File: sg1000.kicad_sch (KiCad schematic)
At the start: 65 parts, among them CN1 Conn_01x07_Female, J1 USB-B1HSB6, J2 RCJ-014, J3 RCJ-013, Q1 2n4401, Q1c1 2n3906, SW1 Pause Key, SW2 Power Toggle, U1 SG-1000-Cart, U10 PLCCZ80, U100 74HCT574, U101 74HCT574, U102 74HCT574, U103 AS6C62256-DIP, U11 AS6C62256-DIP, U12 TMS9918A, U13 74LS139, U16 74LS32, U18 74LS257, U2 SG-1000-Expansion, U21 74LS257, U3 SN76489AN, U99 74HCT04, X2 10.73863MHz

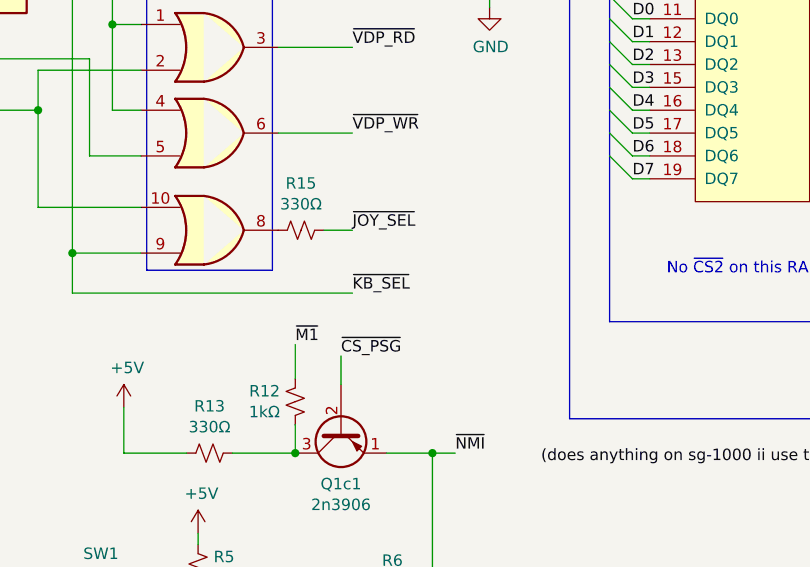
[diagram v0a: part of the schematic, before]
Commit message: Hook up KBSEL
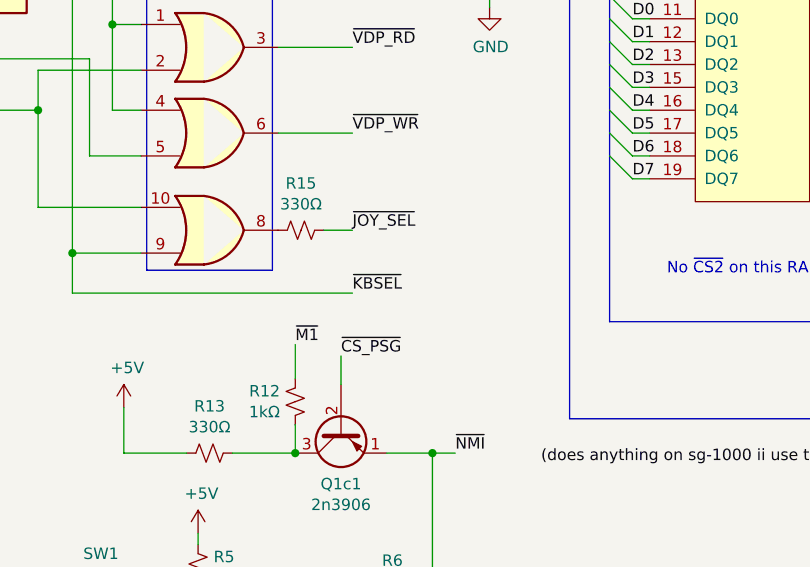
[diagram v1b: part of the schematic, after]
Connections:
- net ~{KB_SEL} is gone; now on net ~{KBSEL}: U13.9 (O3), U16.9
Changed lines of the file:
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@@
     (effects (font (size 1.27 1.27)) (justify right bottom))
   )
-  (label "~{KB_SEL}" (at 111.125 147.32 0)
+  (label "~{KBSEL}" (at 111.125 147.32 0)
     (effects (font (size 1.27 1.27)) (justify left bottom))
   )

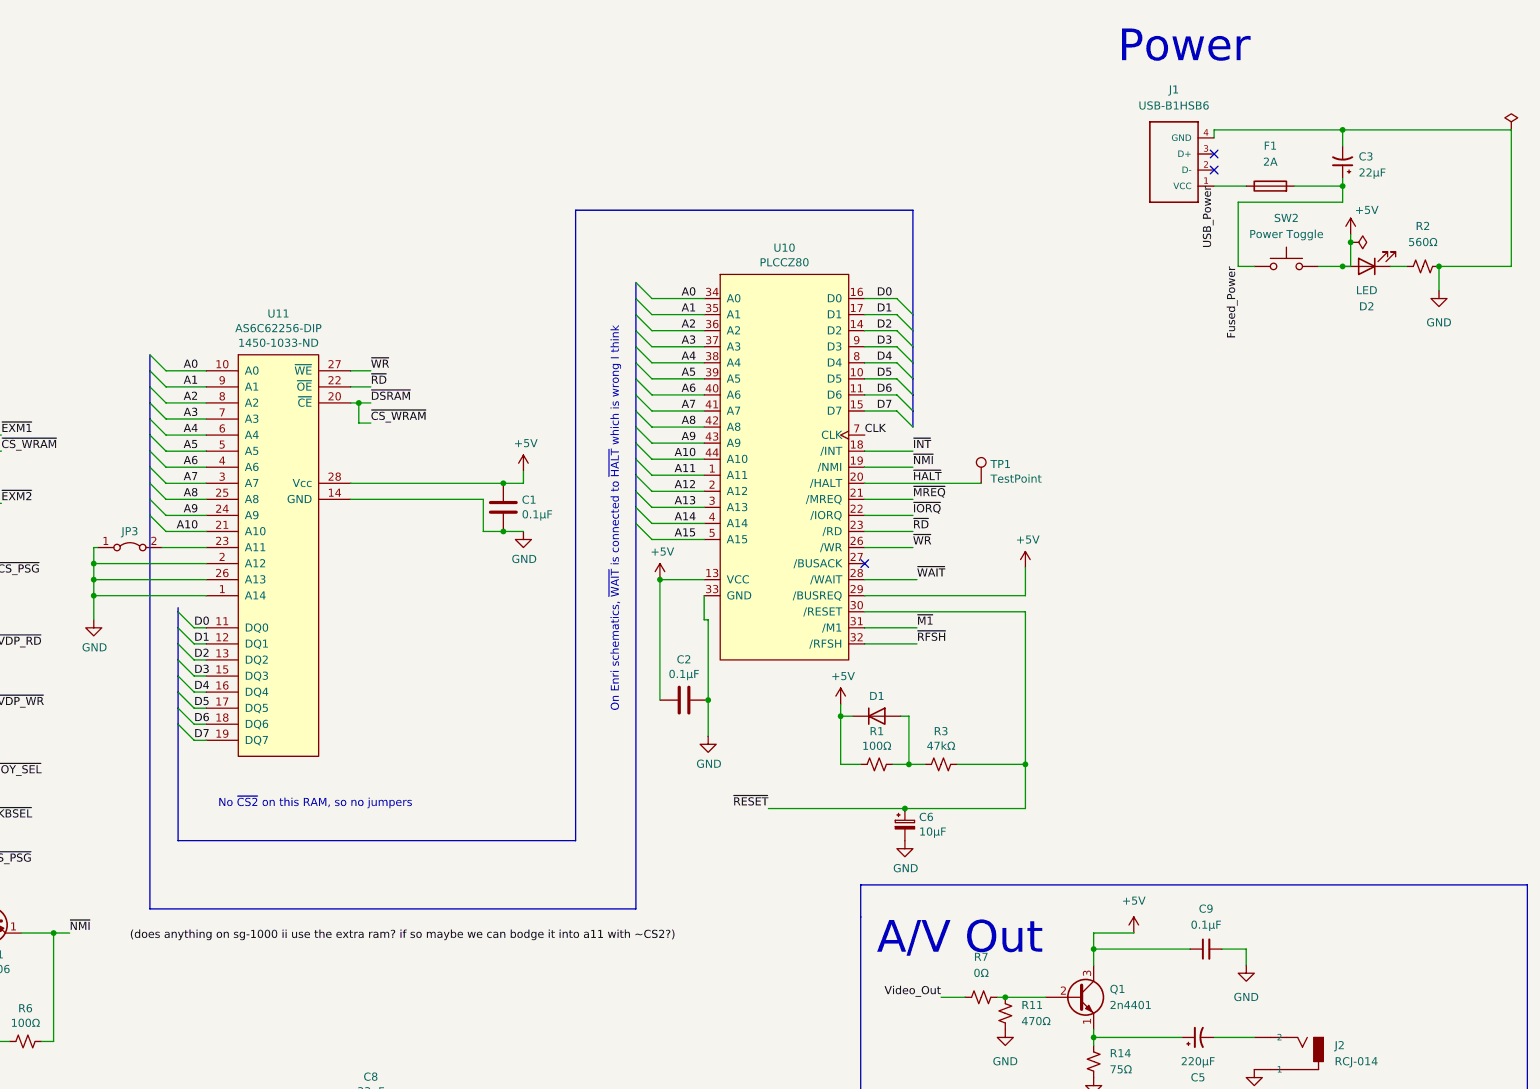
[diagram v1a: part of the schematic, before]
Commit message: Fix many pin warnings
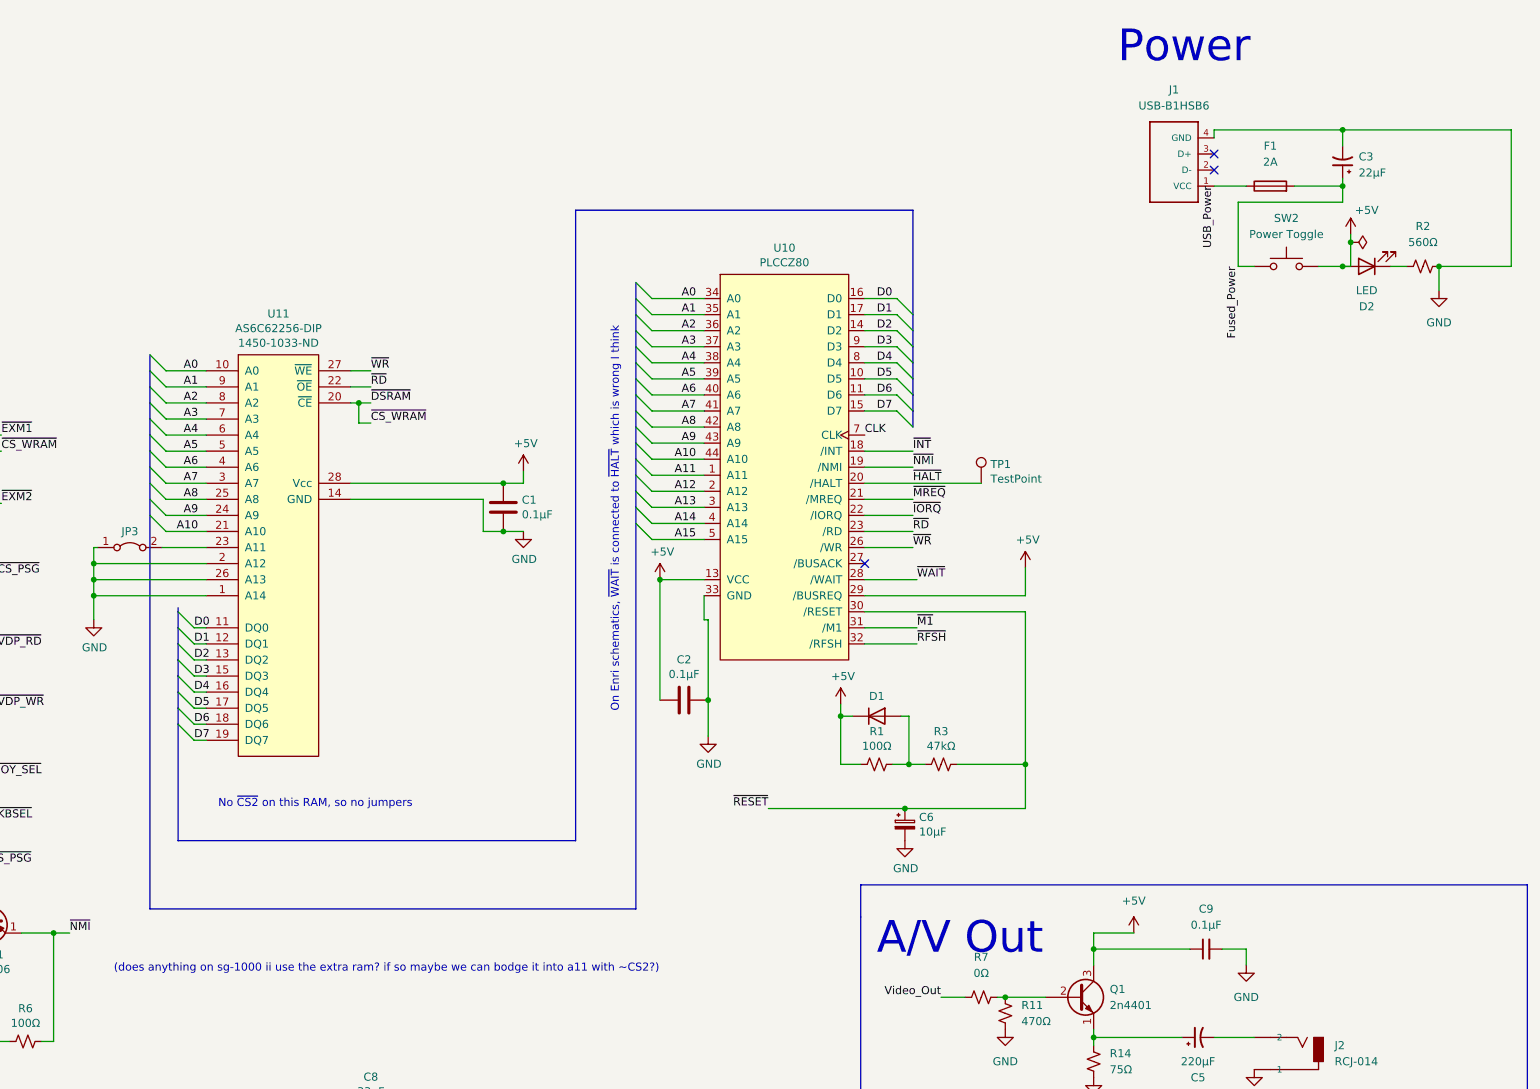
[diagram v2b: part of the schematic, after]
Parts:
- J1: footprint USB-B1HSB6:OST_USB-B1HSB6 -> OST_USB-B1HSB6
- U103, U11: footprint Package_DIP:DIP-28_W15.24mm_Socket_LongPads -> Housings_DIP:DIP-28_W15.24mm_Socket_LongPads
- U12: footprint Package_DIP:DIP-40_W15.24mm_Socket_LongPads -> Housings_DIP:DIP-40_W15.24mm_Socket_LongPads
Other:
- note added: "(does anything on sg-1000 ii use the extra ram? if so maybe we can bodge it into a11 with ~CS2?)"
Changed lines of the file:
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@@
     (effects (font (size 5.0038 5.0038)) (justify left bottom))
   )
+  (text "(does anything on sg-1000 ii use the extra ram? if so maybe we can bodge it into a11 with ~CS2?)"
+    (at 129.54 171.45 0)
+    (effects (font (size 1.27 1.27)) (justify left bottom))
+  )
   (text "A/V Out" (at 250.19 168.91 0)
     (effects (font (size 5.0038 5.0038)) (justify left bottom))
@@
     (effects (font (size 1.27 1.27)) (justify left bottom))
   )
-  (label "(does anything on sg-1000 ii use the extra ram? if so maybe we can bodge it into a11 with ~CS2?)"
-    (at 132.08 166.37 0)
-    (effects (font (size 1.27 1.27)) (justify left bottom))
-  )
   (label "Video_Out" (at 228.6 217.805 0)
     (effects (font (size 1.27 1.27)) (justify left bottom))
@@
     (property "Reference" "U12" (id 0) (at 145.415 203.835 0))
     (property "Value" "TMS9918A" (id 1) (at 145.415 206.1464 0))
-    (property "Footprint" "Package_DIP:DIP-40_W15.24mm_Socket_LongPads" (id 2) (at 145.415 204.47 0)
+    (property "Footprint" "Housings_DIP:DIP-40_W15.24mm_Socket_LongPads" (id 2) (at 145.415 204.47 0)
       (effects (font (size 1.27 1.27)) hide)
     )
-    (property "Datasheet" "" (id 3) (at 145.415 204.47 0)
+    (property "Datasheet" "https://ia803006.us.archive.org/33/items/Texas_Instruments_TMS9918A/Texas_Instruments_TMS9918A_text.pdf" (id 3) (at 145.415 204.47 0)
       (effects (font (size 1.27 1.27)) hide)
     )
@@
       (effects (font (size 1.27 1.27)) hide)
     )
-    (property "Datasheet" "http://www.ti.com/lit/gpn/sn74LS139" (id 3) (at 67.31 83.82 0)
+    (property "Datasheet" "http://www.ti.com/lit/ds/symlink/sn74ls139a.pdf" (id 3) (at 67.31 83.82 0)
       (effects (font (size 1.27 1.27)) hide)
     )
@@
       (effects (font (size 1.27 1.27)) hide)
     )
-    (property "Datasheet" "http://www.ti.com/lit/gpn/sn74LS139" (id 3) (at 67.31 108.585 0)
+    (property "Datasheet" "http://www.ti.com/lit/ds/symlink/sn74ls139a.pdf" (id 3) (at 67.31 108.585 0)
       (effects (font (size 1.27 1.27)) hide)
     )
@@
       (effects (font (size 1.27 1.27)) hide)
     )
-    (property "Datasheet" "http://www.ti.com/lit/gpn/sn74LS139" (id 3) (at 47.625 149.86 0)
+    (property "Datasheet" "http://www.ti.com/lit/ds/symlink/sn74ls139a.pdf" (id 3) (at 47.625 149.86 0)
       (effects (font (size 1.27 1.27)) hide)
     )
@@
     (property "Reference" "U11" (id 0) (at 155.575 67.183 0))
     (property "Value" "AS6C62256-DIP" (id 1) (at 155.575 69.4944 0))
-    (property "Footprint" "Package_DIP:DIP-28_W15.24mm_Socket_LongPads" (id 2) (at 155.575 72.39 0)
+    (property "Footprint" "Housings_DIP:DIP-28_W15.24mm_Socket_LongPads" (id 2) (at 155.575 72.39 0)
       (effects (font (size 1.27 1.27)) hide)
     )
@@
     (property "Reference" "J1" (id 0) (at 297.18 31.75 0))
     (property "Value" "USB-B1HSB6" (id 1) (at 297.18 34.29 0))
-    (property "Footprint" "USB-B1HSB6:OST_USB-B1HSB6" (id 2) (at 300.99 44.45 0)
+    (property "Footprint" "OST_USB-B1HSB6" (id 2) (at 300.99 44.45 0)
       (effects (font (size 1.27 1.27)) (justify left bottom) hide)
     )
@@
     (property "Reference" "U103" (id 0) (at 50.8 205.74 0))
     (property "Value" "AS6C62256-DIP" (id 1) (at 50.8 208.28 0))
-    (property "Footprint" "Package_DIP:DIP-28_W15.24mm_Socket_LongPads" (id 2) (at 50.8 212.09 0)
+    (property "Footprint" "Housings_DIP:DIP-28_W15.24mm_Socket_LongPads" (id 2) (at 50.8 212.09 0)
       (effects (font (size 1.27 1.27)) hide)
     )
@@
     (pin "1")
   )
-  (symbol (lib_id "power:PWR_FLAG") (at 350.52 38.1 0) (unit 1)
-    (in_bom yes) (on_board yes) (fields_autoplaced)
-    (property "Reference" "#FLG0101" (id 0) (at 350.52 36.195 0)
-      (effects (font (size 1.27 1.27)) hide)
-    )
-    (property "Value" "PWR_FLAG" (id 1) (at 350.52 33.02 0)
-      (effects (font (size 1.27 1.27)) hide)
-    )
-    (property "Footprint" "" (id 2) (at 350.52 38.1 0)
-      (effects (font (size 1.27 1.27)) hide)
-    )
-    (property "Datasheet" "~" (id 3) (at 350.52 38.1 0)
-      (effects (font (size 1.27 1.27)) hide)
-    )
-    (pin "1")
-  )
   (symbol (lib_id "74xx:74HCT04") (at 146.05 276.86 0) (unit 1)
     (in_bom yes) (on_board yes) (fields_autoplaced)
@@
   )
   (symbol_instances
-    (path "/b173aa33-db53-42d1-9f49-64e3c773d023"
-      (reference "#FLG0101") (unit 1) (value "PWR_FLAG") (footprint "")
-    )
     (path "/785eb381-512a-4e29-9ab1-d2c5f2c45242"
       (reference "#FLG0102") (unit 1) (value "PWR_FLAG") (footprint "")
@@
     )
     (path "/29d819aa-b433-48a1-9c7f-65135350c51c"
-      (reference "J1") (unit 1) (value "USB-B1HSB6") (footprint "USB-B1HSB6:OST_USB-B1HSB6")
+      (reference "J1") (unit 1) (value "USB-B1HSB6") (footprint "OST_USB-B1HSB6")
     )
     (path "/8dd54862-df4e-4faf-bdd6-951ae815871e"
@@
     )
     (path "/00000000-0000-0000-0000-00006238883d"
-      (reference "U11") (unit 1) (value "AS6C62256-DIP") (footprint "Package_DIP:DIP-28_W15.24mm_Socket_LongPads")
+      (reference "U11") (unit 1) (value "AS6C62256-DIP") (footprint "Housings_DIP:DIP-28_W15.24mm_Socket_LongPads")
     )
     (path "/00000000-0000-0000-0000-00006217e4dc"
-      (reference "U12") (unit 1) (value "TMS9918A") (footprint "Package_DIP:DIP-40_W15.24mm_Socket_LongPads")
+      (reference "U12") (unit 1) (value "TMS9918A") (footprint "Housings_DIP:DIP-40_W15.24mm_Socket_LongPads")
     )
     (path "/00000000-0000-0000-0000-00006223f346"
@@
     )
     (path "/721b9f9a-3f09-4f85-8c9e-cc410a2fa72c"
-      (reference "U103") (unit 1) (value "AS6C62256-DIP") (footprint "Package_DIP:DIP-28_W15.24mm_Socket_LongPads")
+      (reference "U103") (unit 1) (value "AS6C62256-DIP") (footprint "Housings_DIP:DIP-28_W15.24mm_Socket_LongPads")
     )
     (path "/00000000-0000-0000-0000-0000621e9070"

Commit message: Fix diode size
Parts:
- D1: footprint Diode_THT:D_DO-15_P12.70mm_Horizontal -> Diode_THT:D_A-405_P7.62mm_Horizontal
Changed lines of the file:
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@@
       (effects (font (size 1.27 1.27)) hide)
     )
-    (property "Footprint" "Diode_THT:D_DO-15_P12.70mm_Horizontal" (id 2) (at 250.19 130.81 0)
+    (property "Footprint" "Diode_THT:D_A-405_P7.62mm_Horizontal" (id 2) (at 250.19 130.81 0)
       (effects (font (size 1.27 1.27)) hide)
     )
@@
     )
     (path "/00000000-0000-0000-0000-00006219586d"
-      (reference "D1") (unit 1) (value "D") (footprint "Diode_THT:D_DO-15_P12.70mm_Horizontal")
+      (reference "D1") (unit 1) (value "D") (footprint "Diode_THT:D_A-405_P7.62mm_Horizontal")
     )
     (path "/d54174c4-a10b-46aa-b80a-ed73777cda6c"

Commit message: Fix /EXM2 being severed from cart
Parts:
- added JP?: SolderJumper_2_Bridged, Jumper:SolderJumper-2_P1.3mm_Bridged_RoundedPad1.0x1.5mm, symbol Jumper:SolderJumper_2_Bridged
- R9: value 540Ω -> 560Ω
- RN1, RN2: DigiKey (none) -> 4607X-101-472LF-ND
- U13: DigiKey (none) -> 296-1640-5-ND
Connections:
- net ~{EXM2}: now also JP?.1 (A)
- net at JP1.2 (B), U1.B19 (~{EXM2}): now also JP?.2 (B)
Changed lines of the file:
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@@
   (junction (at 106.68 460.375) (diameter 0) (color 0 0 0 0)
   )
+  (junction (at 38.1 562.61) (diameter 0) (color 0 0 0 0)
+  )
   (junction (at 126.365 109.22) (diameter 0) (color 0 0 0 0)
   )
@@
     (stroke (width 0) (type default) (color 0 0 0 0))
   )
+  (wire (pts (xy 22.86 568.96) (xy 25.4 568.96))
+    (stroke (width 0) (type default) (color 0 0 0 0))
+  )
   (wire (pts (xy 45.085 365.76) (xy 52.705 365.76))
     (stroke (width 0) (type default) (color 0 0 0 0))
@@
     (stroke (width 0) (type default) (color 0 0 0 0))
   )
+  (wire (pts (xy 33.02 568.96) (xy 38.1 568.96))
+    (stroke (width 0) (type default) (color 0 0 0 0))
+  )
   (wire (pts (xy 92.075 379.095) (xy 92.075 371.475))
     (stroke (width 0) (type default) (color 0 0 0 0))
@@
     (stroke (width 0) (type default) (color 0 0 0 0))
   )
+  (wire (pts (xy 38.1 568.96) (xy 38.1 562.61))
+    (stroke (width 0) (type default) (color 0 0 0 0))
+  )
   (wire (pts (xy 111.125 120.015) (xy 102.87 120.015))
     (stroke (width 0) (type default) (color 0 0 0 0))
@@
     (stroke (width 0) (type default) (color 0 0 0 0))
   )
+  (wire (pts (xy 38.1 562.61) (xy 43.18 562.61))
+    (stroke (width 0) (type default) (color 0 0 0 0))
+  )
   (wire (pts (xy 269.24 175.26) (xy 270.51 175.26))
     (stroke (width 0) (type default) (color 0 0 0 0))
@@
     (stroke (width 0) (type default) (color 0 0 0 0))
   )
-  (wire (pts (xy 33.02 562.61) (xy 43.18 562.61))
+  (wire (pts (xy 33.02 562.61) (xy 38.1 562.61))
     (stroke (width 0) (type default) (color 0 0 0 0))
   )
@@
     (effects (font (size 1.27 1.27)) (justify left bottom))
   )
+  (label "~{EXM2}" (at 22.86 568.96 180)
+    (effects (font (size 1.27 1.27)) (justify right bottom))
+  )
   (label "AD3" (at 132.715 224.79 180)
     (effects (font (size 1.27 1.27)) (justify right bottom))
@@
       (effects (font (size 1.27 1.27)) hide)
     )
+    (property "DigiKey" "296-1640-5-ND" (id 4) (at 67.31 108.585 0)
+      (effects (font (size 1.27 1.27)) hide)
+    )
     (pin "10")
     (pin "11")
@@
     (in_bom yes) (on_board yes)
     (property "Reference" "R9" (id 0) (at 100.965 90.805 90))
-    (property "Value" "540Ω" (id 1) (at 100.965 93.345 90))
+    (property "Value" "560Ω" (id 1) (at 100.965 93.345 90))
     (property "Footprint" "Resistor_SMD:R_0805_2012Metric_Pad1.20x1.40mm_HandSolder" (id 2) (at 100.965 88.9 0)
       (effects (font (size 1.27 1.27)) hide)
@@
       (effects (font (size 1.27 1.27)) hide)
     )
+    (property "DigiKey" "4607X-101-472LF-ND" (id 4) (at 97.155 366.395 0)
+      (effects (font (size 1.27 1.27)) hide)
+    )
     (pin "1")
     (pin "2")
@@
       (effects (font (size 1.27 1.27)) hide)
     )
+    (property "DigiKey" "4607X-101-472LF-ND" (id 4) (at 111.76 444.5 0)
+      (effects (font (size 1.27 1.27)) hide)
+    )
     (pin "1")
     (pin "2")
@@
     (pin "1")
   )
+  (symbol (lib_id "Jumper:SolderJumper_2_Bridged") (at 29.21 568.96 0) (unit 1)
+    (in_bom yes) (on_board yes)
+    (property "Reference" "JP?" (id 0) (at 29.21 572.77 0))
+    (property "Value" "SolderJumper_2_Bridged" (id 1) (at 29.21 565.15 0)
+      (effects (font (size 1.27 1.27)) hide)
+    )
+    (property "Footprint" "Jumper:SolderJumper-2_P1.3mm_Bridged_RoundedPad1.0x1.5mm" (id 2) (at 29.21 568.96 0)
+      (effects (font (size 1.27 1.27)) hide)
+    )
+    (property "Datasheet" "~" (id 3) (at 29.21 568.96 0)
+      (effects (font (size 1.27 1.27)) hide)
+    )
+    (pin "1")
+    (pin "2")
+  )
   (symbol (lib_id "Device:R_Small_US") (at 284.48 185.42 0) (unit 1)
     (in_bom yes) (on_board yes) (fields_autoplaced)
@@
       (reference "JP3") (unit 1) (value "Jumper_2_Bridged") (footprint "Jumper:SolderJumper-2_P1.3mm_Bridged2Bar_RoundedPad1.0x1.5mm")
     )
+    (path "/97d6fcd3-ceba-42ac-b87a-8d981d14ecab"
+      (reference "JP?") (unit 1) (value "SolderJumper_2_Bridged") (footprint "Jumper:SolderJumper-2_P1.3mm_Bridged_RoundedPad1.0x1.5mm")
+    )
     (path "/e8ff5aa1-c73d-405b-ae17-444be3e4dae0"
       (reference "Q1") (unit 1) (value "2n4401") (footprint "Package_TO_SOT_THT:TO-92_Inline_Wide")
@@
     )
     (path "/00000000-0000-0000-0000-0000622a26f4"
-      (reference "R9") (unit 1) (value "540Ω") (footprint "Resistor_SMD:R_0805_2012Metric_Pad1.20x1.40mm_HandSolder")
+      (reference "R9") (unit 1) (value "560Ω") (footprint "Resistor_SMD:R_0805_2012Metric_Pad1.20x1.40mm_HandSolder")
     )
     (path "/7e64581d-ac7c-4e97-9f0b-a7127da87491"
